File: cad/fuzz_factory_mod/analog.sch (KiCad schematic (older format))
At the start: 25 parts

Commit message: Continued schematic
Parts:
- removed C?: 100n, symbol Device:C
- removed R?: 220k, symbol Device:R
- added C?: 10u, symbol Device:CP
- added C?: 100n, symbol Device:C
- added RV? (x2): 10k, symbol Device:R_POT_TRIM
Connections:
- net labels added: IN_AUDIO
- wire segments 93 -> 100
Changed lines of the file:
@@
-$EndComp
-$Comp
-L Device:C C?
-U 1 1 5DF91F08
-P 4750 4500
-F 0 "C?" V 4498 4500 50  0000 C CNN
-F 1 "100n" V 4589 4500 50  0000 C CNN
-F 2 "" H 4788 4350 50  0001 C CNN
-F 3 "~" H 4750 4500 50  0001 C CNN
-	1    4750 4500
-	0    1    1    0
-$EndComp
-$Comp
-L Device:R R?
-U 1 1 5DF92795
-P 4250 4500
-F 0 "R?" V 4043 4500 50  0000 C CNN
-F 1 "220k" V 4134 4500 50  0000 C CNN
-F 2 "" V 4180 4500 50  0001 C CNN
-F 3 "~" H 4250 4500 50  0001 C CNN
-	1    4250 4500
-	0    1    1    0
 $EndComp
 $Comp
@@
 $EndComp
 Wire Wire Line
-	4400 4500 4600 4500
-Wire Wire Line
 	4900 4500 5000 4500
 Wire Wire Line
@@
 Connection ~ 5000 4500
 Wire Wire Line
-	5000 4500 5200 4500
+	5000 4500 5100 4500
 Wire Wire Line
 	5000 3800 5000 4000
@@
 Wire Wire Line
 	7500 3100 7500 3000
-Wire Wire Line
-	7500 3000 7100 3000
 Connection ~ 7000 3000
 Wire Wire Line
 	7500 3400 7500 3500
-Wire Wire Line
-	7500 3500 7300 3500
 Connection ~ 7000 3500
 Wire Wire Line
 	7000 3500 7000 3600
-Text HLabel 8500 2800 2    50   Input ~ 0
+Text HLabel 1500 7000 0    50   Input ~ 0
 GAIN_POT_1
-Text HLabel 8500 2900 2    50   Input ~ 0
+Text HLabel 1500 7100 0    50   Input ~ 0
 GAIN_POT_2
-Text HLabel 8500 3000 2    50   Input ~ 0
+Text HLabel 1500 7200 0    50   Input ~ 0
 GAIN_POT_3
 Connection ~ 7000 4000
@@
 Wire Wire Line
 	7000 4000 8000 4000
-Text HLabel 8500 2700 2    50   Input ~ 0
+Text HLabel 1500 6500 0    50   Input ~ 0
 COMP_POT_1
-Text HLabel 8500 3100 2    50   Input ~ 0
+Text HLabel 1500 6600 0    50   Input ~ 0
 COMP_POT_2
-Wire Wire Line
-	8500 2700 8000 2700
-Wire Wire Line
-	8000 2700 8000 3000
-Connection ~ 8000 3000
-Wire Wire Line
-	8500 3100 8400 3100
-Wire Wire Line
-	8400 3100 8400 4000
-Wire Wire Line
-	8400 4000 8300 4000
-Connection ~ 8000 4000
-Wire Wire Line
-	8500 2800 7100 2800
-Wire Wire Line
-	7100 2800 7100 3000
-Connection ~ 7100 3000
-Wire Wire Line
-	7100 3000 7000 3000
-Wire Wire Line
-	8500 2900 7300 2900
-Wire Wire Line
-	7300 2900 7300 3500
-Connection ~ 7300 3500
-Wire Wire Line
-	7300 3500 7000 3500
-Wire Wire Line
-	8500 3000 8300 3000
-Wire Wire Line
-	8300 3000 8300 4000
-Connection ~ 8300 4000
-Wire Wire Line
-	8300 4000 8000 4000
 Text Notes 7050 3150 0    50   ~ 0
 DNP
@@
 	7000 5900 7000 6000
 Wire Wire Line
-	6400 5400 6400 5600
-Wire Wire Line
 	6400 6000 7000 6000
 Connection ~ 7000 6000
@@
 Wire Wire Line
 	7000 5100 7000 5000
-Wire Wire Line
-	6400 4900 6400 5000
 Text Notes 7950 3350 1    50   ~ 0
 COMP
@@
 Text HLabel 8500 5200 2    50   Input ~ 0
 VOLUME_POT_3
-Text HLabel 6000 5500 0    50   Input ~ 0
+Text HLabel 1500 6000 0    50   Input ~ 0
 GATE_POT_1
-Text HLabel 6000 5600 0    50   Input ~ 0
+Text HLabel 1500 6100 0    50   Input ~ 0
 GATE_POT_2
-Wire Wire Line
-	6000 5500 6100 5500
-Wire Wire Line
-	6100 5500 6100 5000
-Wire Wire Line
-	6100 5000 6400 5000
-Connection ~ 6400 5000
-Wire Wire Line
-	6400 5000 6400 5100
-Wire Wire Line
-	6000 5600 6400 5600
-Connection ~ 6400 5600
-Wire Wire Line
-	6400 5600 6400 6000
 Wire Wire Line
 	8500 5000 7000 5000
@@
 Wire Wire Line
 	5750 2300 5750 2600
+$Comp
+L Device:R_POT_TRIM RV?
+U 1 1 5DF4B057
+P 2000 3650
+F 0 "RV?" H 1930 3696 50  0000 R CNN
+F 1 "10k" H 1930 3605 50  0000 R CNN
+F 2 "" H 2000 3650 50  0001 C CNN
+F 3 "~" H 2000 3650 50  0001 C CNN
+	1    2000 3650
+	1    0    0    -1
+$EndComp
+Wire Wire Line
+	2000 3800 2000 3850
+Wire Wire Line
+	2150 3650 2200 3650
+Wire Wire Line
+	2200 3650 2200 3850
+Wire Wire Line
+	2200 3850 2000 3850
+Connection ~ 2000 3850
+Text Label 8100 4000 0    50   ~ 0
+COMP_POT_2
+Wire Wire Line
+	7000 3500 7500 3500
+Wire Wire Line
+	7000 3000 7500 3000
+Wire Wire Line
+	8000 4000 8600 4000
+Connection ~ 8000 4000
+Wire Wire Line
+	8000 3000 8600 3000
+Connection ~ 8000 3000
+Text Label 8100 3000 0    50   ~ 0
+COMP_POT_1
+Text Label 7100 3000 0    50   ~ 0
+GAIN_POT_1
+Text Label 7100 3500 0    50   ~ 0
+GAIN_POT_2
+Text Label 7100 4000 0    50   ~ 0
+GAIN_POT_3
+Wire Wire Line
+	6400 4900 6400 5100
+Wire Wire Line
+	6400 5400 6400 6000
+Text Label 6400 5000 0    50   ~ 0
+GATE_POT_1
+Text Label 6400 5500 0    50   ~ 0
+GATE_POT_2
+$Comp
+L Device:CP C?
+U 1 1 5DF7EFC6
+P 4750 4500
+F 0 "C?" H 4868 4546 50  0000 L CNN
+F 1 "10u" H 4868 4455 50  0000 L CNN
+F 2 "" H 4788 4350 50  0001 C CNN
+F 3 "~" H 4750 4500 50  0001 C CNN
+	1    4750 4500
+	0    1    1    0
+$EndComp
+$Comp
+L Device:C C?
+U 1 1 5DF8CBCE
+P 4750 4900
+F 0 "C?" V 4498 4900 50  0000 C CNN
+F 1 "100n" V 4589 4900 50  0000 C CNN
+F 2 "" H 4788 4750 50  0001 C CNN
+F 3 "~" H 4750 4900 50  0001 C CNN
+	1    4750 4900
+	0    -1   -1   0
+$EndComp
+Wire Wire Line
+	4500 4500 4600 4500
+Wire Wire Line
+	4600 4900 4500 4900
+Wire Wire Line
+	4500 4900 4500 4500
+Wire Wire Line
+	4900 4900 5100 4900
+Wire Wire Line
+	5100 4900 5100 4500
+Connection ~ 5100 4500
+Wire Wire Line
+	5100 4500 5200 4500
+Text HLabel 4400 4500 0    50   Input ~ 0
+IN_AUDIO
+Wire Wire Line
+	4400 4500 4500 4500
+Connection ~ 4500 4500
+Text Label 2000 3400 1    50   ~ 0
+COMP_POT_1
+Text Label 2000 3950 3    50   ~ 0
+COMP_POT_2
+$Comp
+L Device:R_POT_TRIM RV?
+U 1 1 5DF95B54
+P 3000 3650
+F 0 "RV?" H 2930 3696 50  0000 R CNN
+F 1 "10k" H 2930 3605 50  0000 R CNN
+F 2 "" H 3000 3650 50  0001 C CNN
+F 3 "~" H 3000 3650 50  0001 C CNN
+	1    3000 3650
+	1    0    0    -1
+$EndComp
+Wire Wire Line
+	3000 3800 3000 3850
+Wire Wire Line
+	3150 3650 3200 3650
+Wire Wire Line
+	3200 3650 3200 3850
+Wire Wire Line
+	3200 3850 3000 3850
+Connection ~ 3000 3850
+Text Label 3000 3400 1    50   ~ 0
+GATE_POT_1
+Text Label 3000 3950 3    50   ~ 0
+GATE_POT_2
+Text Label 1600 6000 0    50   ~ 0
+GATE_POT_1
+Text Label 1600 6100 0    50   ~ 0
+GATE_POT_2
+Text Label 1600 6500 0    50   ~ 0
+COMP_POT_1
+Text Label 1600 6600 0    50   ~ 0
+COMP_POT_2
+Text Label 1600 7000 0    50   ~ 0
+GAIN_POT_1
+Text Label 1600 7100 0    50   ~ 0
+GAIN_POT_2
+Text Label 1600 7200 0    50   ~ 0
+GAIN_POT_3
+Wire Wire Line
+	1500 6000 2100 6000
+Wire Wire Line
+	1500 6100 2100 6100
+Wire Wire Line
+	1500 6500 2100 6500
+Wire Wire Line
+	1500 6600 2100 6600
+Wire Wire Line
+	1500 7000 2100 7000
+Wire Wire Line
+	1500 7100 2100 7100
+Wire Wire Line
+	1500 7200 2100 7200
+Wire Wire Line
+	2000 3850 2000 4500
+Wire Wire Line
+	3000 3850 3000 4500
+Wire Wire Line
+	2000 3500 2000 2900
+Wire Wire Line
+	3000 3500 3000 2900
 $EndSCHEMATC

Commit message: Continued schematic
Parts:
- added R?: 0, symbol Device:R
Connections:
- net labels added: +9V, IN_PWM_LSB, IN_PWM_LSBn, IN_PWM_MSB, IN_PWM_MSBn, OUT_AUDIO, STARVE_POT_1, STARVE_POT_2
- wire segments 100 -> 109
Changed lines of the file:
@@
 $Descr A4 11693 8268
 encoding utf-8
-Sheet 3 5
+Sheet 3 6
 Title ""
 Date ""
@@
 Wire Wire Line
 	7000 3500 7000 3600
+Text HLabel 1500 6900 0    50   Input ~ 0
+GAIN_POT_1
 Text HLabel 1500 7000 0    50   Input ~ 0
-GAIN_POT_1
+GAIN_POT_2
 Text HLabel 1500 7100 0    50   Input ~ 0
-GAIN_POT_2
-Text HLabel 1500 7200 0    50   Input ~ 0
 GAIN_POT_3
 Connection ~ 7000 4000
@@
 Text Label 1600 6600 0    50   ~ 0
 COMP_POT_2
+Text Label 1600 6900 0    50   ~ 0
+GAIN_POT_1
 Text Label 1600 7000 0    50   ~ 0
-GAIN_POT_1
+GAIN_POT_2
 Text Label 1600 7100 0    50   ~ 0
-GAIN_POT_2
-Text Label 1600 7200 0    50   ~ 0
 GAIN_POT_3
 Wire Wire Line
@@
 	1500 6600 2100 6600
 Wire Wire Line
+	1500 6900 2100 6900
+Wire Wire Line
 	1500 7000 2100 7000
 Wire Wire Line
 	1500 7100 2100 7100
 Wire Wire Line
-	1500 7200 2100 7200
-Wire Wire Line
 	2000 3850 2000 4500
 Wire Wire Line
@@
 Wire Wire Line
 	3000 3500 3000 2900
+Text HLabel 1300 1600 0    50   Input ~ 0
+IN_PWM_LSB
+Text HLabel 1300 1700 0    50   Input ~ 0
+IN_PWM_LSBn
+Text HLabel 1300 1800 0    50   Input ~ 0
+IN_PWM_MSB
+Text HLabel 1300 1900 0    50   Input ~ 0
+IN_PWM_MSBn
+Wire Wire Line
+	1500 1600 1300 1600
+Wire Wire Line
+	1300 1700 1500 1700
+Wire Wire Line
+	1500 1800 1300 1800
+Wire Wire Line
+	1300 1900 1500 1900
+$Comp
+L power:+9V #PWR?
+U 1 1 5E01411F
+P 5750 1000
+F 0 "#PWR?" H 5750 850 50  0001 C CNN
+F 1 "+9V" H 5765 1173 50  0000 C CNN
+F 2 "" H 5750 1000 50  0001 C CNN
+F 3 "" H 5750 1000 50  0001 C CNN
+	1    5750 1000
+	1    0    0    -1
+$EndComp
+$Comp
+L Device:R R?
+U 1 1 5E015714
+P 5750 1250
+F 0 "R?" H 5820 1296 50  0000 L CNN
+F 1 "0" H 5820 1205 50  0000 L CNN
+F 2 "" V 5680 1250 50  0001 C CNN
+F 3 "~" H 5750 1250 50  0001 C CNN
+	1    5750 1250
+	1    0    0    -1
+$EndComp
+Wire Wire Line
+	5750 1400 5750 1500
+Connection ~ 5750 1500
+Wire Wire Line
+	5750 1100 5750 1000
+Text Label 5850 1700 0    50   ~ 0
+STARVE_POT_1
+Text Label 5850 2300 0    50   ~ 0
+STARVE_POT_2
+Text Label 1600 7500 0    50   ~ 0
+STARVE_POT_1
+Text Label 1600 7600 0    50   ~ 0
+STARVE_POT_2
+Text HLabel 1500 7500 0    50   Input ~ 0
+STARVE_POT_1
+Text HLabel 1500 7600 0    50   Input ~ 0
+STARVE_POT_2
+Wire Wire Line
+	1500 7500 2100 7500
+Wire Wire Line
+	1500 7600 2100 7600
+Text HLabel 8500 5500 2    50   Input ~ 0
+OUT_AUDIO
+Wire Wire Line
+	8000 5500 8500 5500
+Connection ~ 8000 5500
+$Sheet
+S 7150 800  950  600
+U 5E0DD00B
+F0 "Digipot" 50
+F1 "DIGIPOT.sch" 50
+$EndSheet
 $EndSCHEMATC

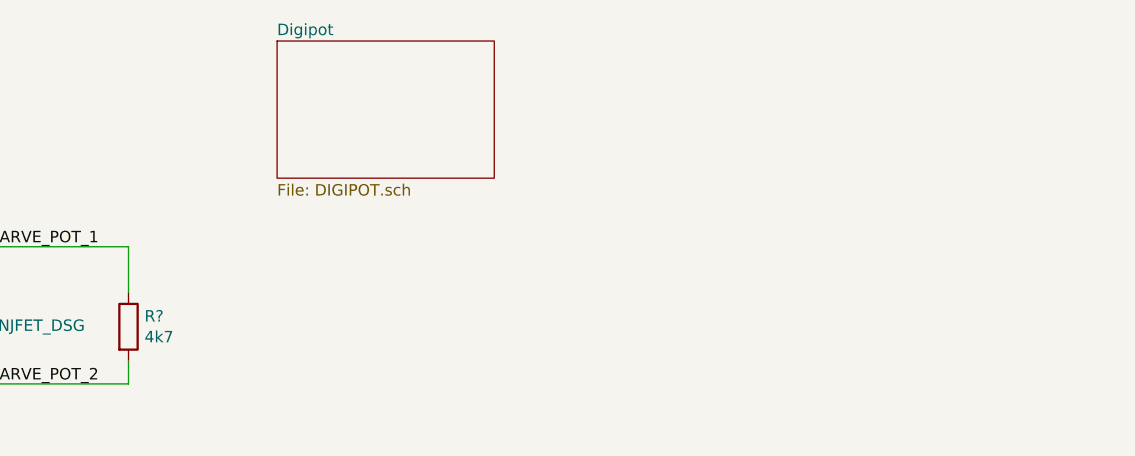
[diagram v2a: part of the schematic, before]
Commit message: Continued schematic.
Added PSU and interface from tremolo project.
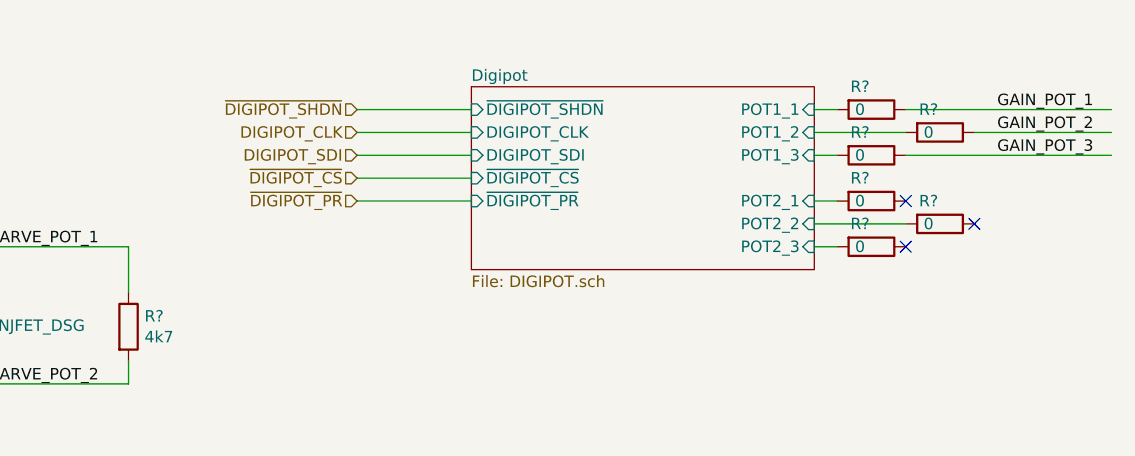
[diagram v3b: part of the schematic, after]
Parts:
- added R? (x6): 0, symbol Device:R
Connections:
- net labels added: DIGIPOT_CLK, DIGIPOT_SDI, ~DIGIPOT_CS, ~DIGIPOT_PR, ~DIGIPOT_SHDN
- wire segments 109 -> 123
- no-connect marks 0 -> 3
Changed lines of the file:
@@
 $Descr A4 11693 8268
 encoding utf-8
-Sheet 3 6
+Sheet 3 11
 Title ""
 Date ""
@@
 Connection ~ 8000 5500
 $Sheet
-S 7150 800  950  600
+S 8000 1000 1500 800
 U 5E0DD00B
 F0 "Digipot" 50
 F1 "DIGIPOT.sch" 50
+F2 "~DIGIPOT_SHDN" I L 8000 1100 50
+F3 "DIGIPOT_CLK" I L 8000 1200 50
+F4 "DIGIPOT_SDI" I L 8000 1300 50
+F5 "~DIGIPOT_CS" I L 8000 1400 50
+F6 "~DIGIPOT_PR" I L 8000 1500 50
+F7 "POT1_1" I R 9500 1100 50
+F8 "POT1_2" I R 9500 1200 50
+F9 "POT1_3" I R 9500 1300 50
+F10 "POT2_1" I R 9500 1500 50
+F11 "POT2_2" I R 9500 1600 50
+F12 "POT2_3" I R 9500 1700 50
 $EndSheet
+Text HLabel 7500 1100 0    50   Input ~ 0
+~DIGIPOT_SHDN
+Text HLabel 7500 1200 0    50   Input ~ 0
+DIGIPOT_CLK
+Text HLabel 7500 1300 0    50   Input ~ 0
+DIGIPOT_SDI
+Text HLabel 7500 1400 0    50   Input ~ 0
+~DIGIPOT_CS
+Text HLabel 7500 1500 0    50   Input ~ 0
+~DIGIPOT_PR
+Wire Wire Line
+	7500 1100 8000 1100
+Wire Wire Line
+	8000 1200 7500 1200
+Wire Wire Line
+	7500 1300 8000 1300
+Wire Wire Line
+	8000 1400 7500 1400
+Wire Wire Line
+	7500 1500 8000 1500
+$Comp
+L Device:R R?
+U 1 1 5E37400A
+P 9750 1100
+F 0 "R?" V 9650 1050 50  0000 C CNN
+F 1 "0" V 9750 1050 50  0000 C CNN
+F 2 "" V 9680 1100 50  0001 C CNN
+F 3 "~" H 9750 1100 50  0001 C CNN
+	1    9750 1100
+	0    1    1    0
+$EndComp
+$Comp
+L Device:R R?
+U 1 1 5E374C21
+P 10050 1200
+F 0 "R?" V 9950 1150 50  0000 C CNN
+F 1 "0" V 10050 1150 50  0000 C CNN
+F 2 "" V 9980 1200 50  0001 C CNN
+F 3 "~" H 10050 1200 50  0001 C CNN
+	1    10050 1200
+	0    1    1    0
+$EndComp
+$Comp
+L Device:R R?
+U 1 1 5E3751A9
+P 9750 1300
+F 0 "R?" V 9650 1250 50  0000 C CNN
+F 1 "0" V 9750 1250 50  0000 C CNN
+F 2 "" V 9680 1300 50  0001 C CNN
+F 3 "~" H 9750 1300 50  0001 C CNN
+	1    9750 1300
+	0    1    1    0
+$EndComp
+$Comp
+L Device:R R?
+U 1 1 5E376867
+P 9750 1500
+F 0 "R?" V 9650 1450 50  0000 C CNN
+F 1 "0" V 9750 1450 50  0000 C CNN
+F 2 "" V 9680 1500 50  0001 C CNN
+F 3 "~" H 9750 1500 50  0001 C CNN
+	1    9750 1500
+	0    1    1    0
+$EndComp
+$Comp
+L Device:R R?
+U 1 1 5E376871
+P 10050 1600
+F 0 "R?" V 9950 1550 50  0000 C CNN
+F 1 "0" V 10050 1550 50  0000 C CNN
+F 2 "" V 9980 1600 50  0001 C CNN
+F 3 "~" H 10050 1600 50  0001 C CNN
+	1    10050 1600
+	0    1    1    0
+$EndComp
+$Comp
+L Device:R R?
+U 1 1 5E37687B
+P 9750 1700
+F 0 "R?" V 9650 1650 50  0000 C CNN
+F 1 "0" V 9750 1650 50  0000 C CNN
+F 2 "" V 9680 1700 50  0001 C CNN
+F 3 "~" H 9750 1700 50  0001 C CNN
+	1    9750 1700
+	0    1    1    0
+$EndComp
+Wire Wire Line
+	9600 1100 9500 1100
+Wire Wire Line
+	9500 1200 9900 1200
+Wire Wire Line
+	9600 1300 9500 1300
+Wire Wire Line
+	9600 1500 9500 1500
+Wire Wire Line
+	9500 1600 9900 1600
+Wire Wire Line
+	9600 1700 9500 1700
+Text Label 10300 1100 0    50   ~ 0
+GAIN_POT_1
+Text Label 10300 1200 0    50   ~ 0
+GAIN_POT_2
+Text Label 10300 1300 0    50   ~ 0
+GAIN_POT_3
+Wire Wire Line
+	10200 1200 10800 1200
+Wire Wire Line
+	9900 1100 10800 1100
+Wire Wire Line
+	9900 1300 10800 1300
+NoConn ~ 9900 1500
+NoConn ~ 10200 1600
+NoConn ~ 9900 1700
 $EndSCHEMATC

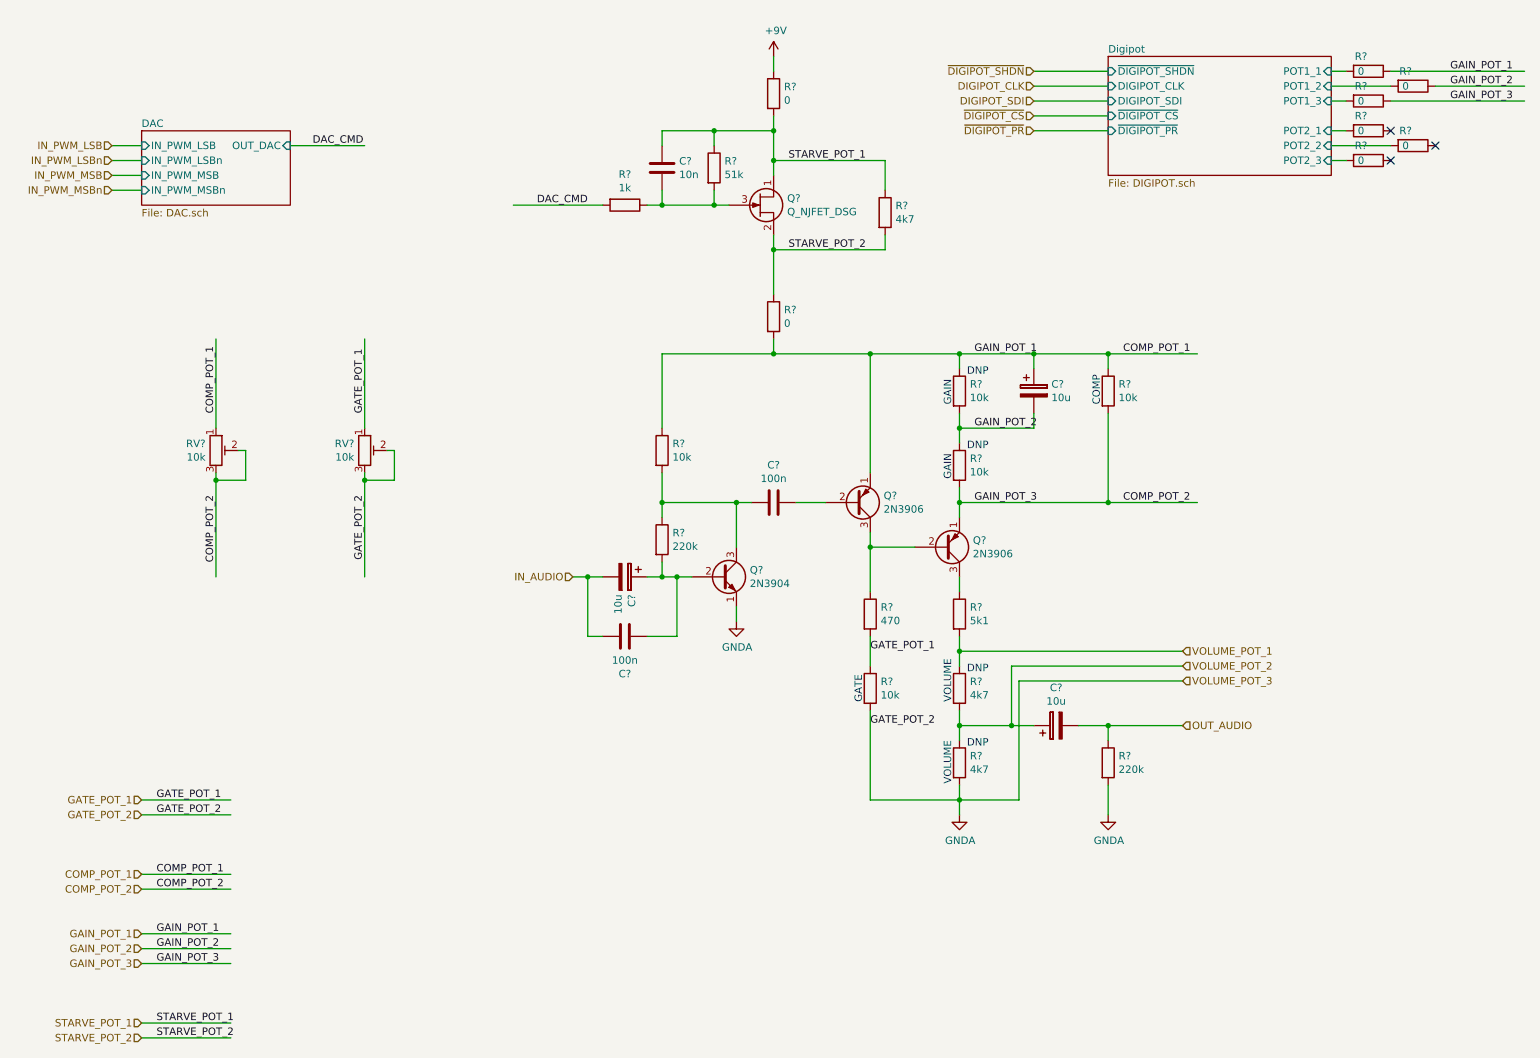
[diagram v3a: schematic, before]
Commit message: Factorised fuzz factory circuit.
Added MIDI interface.
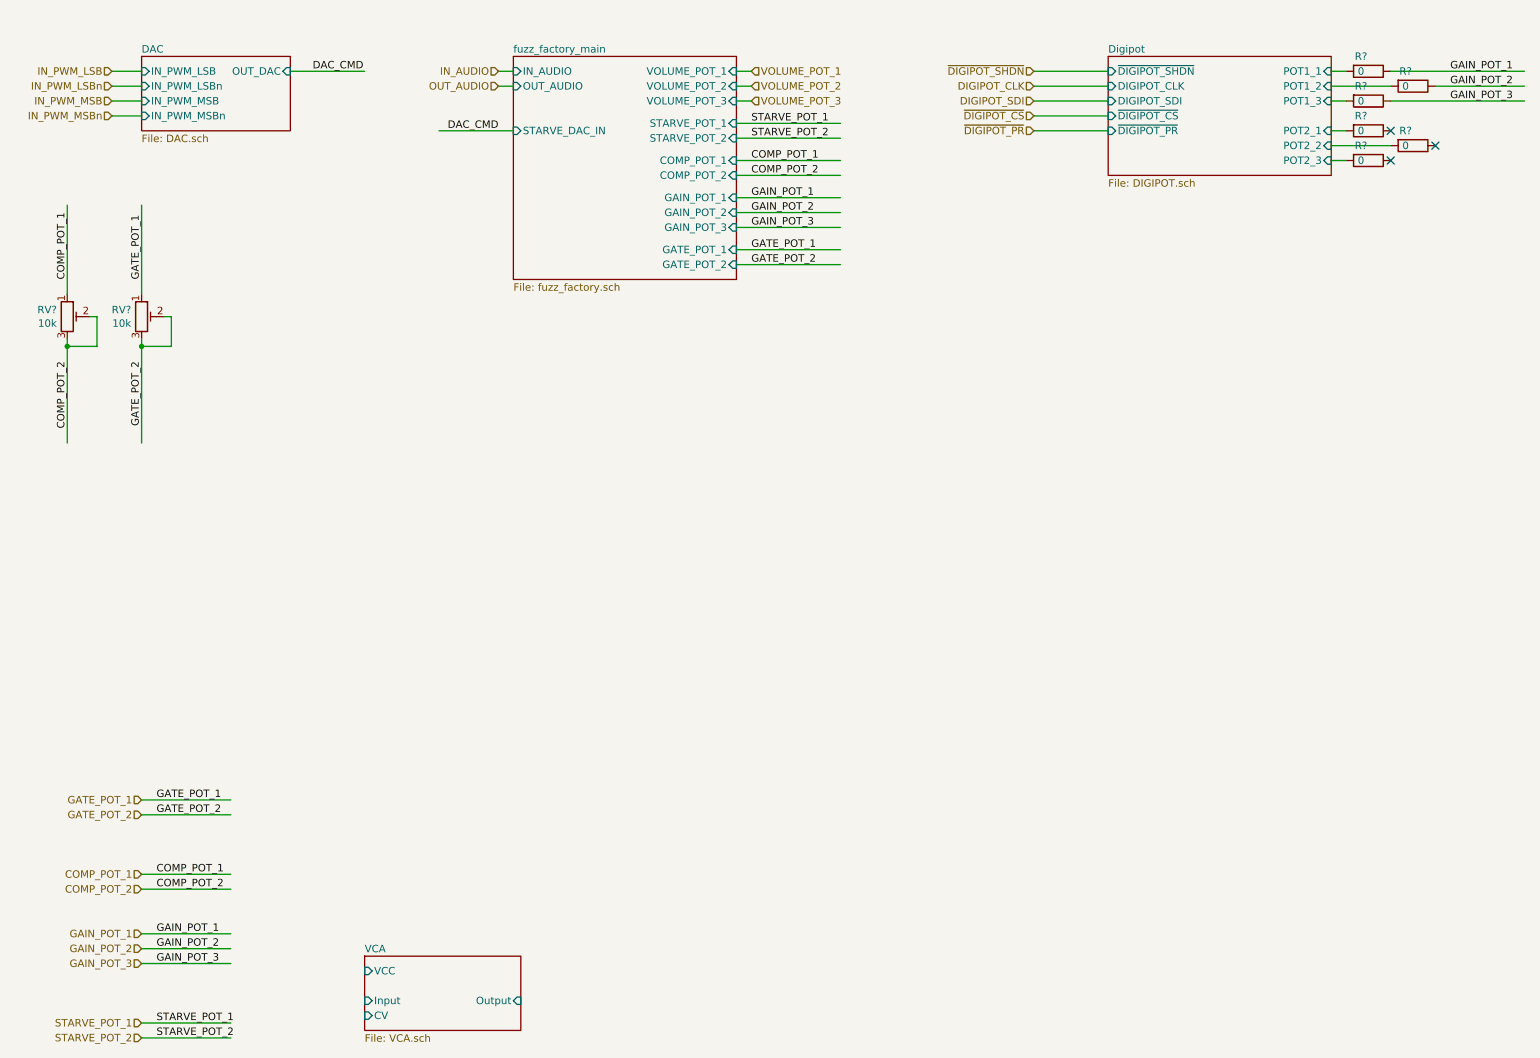
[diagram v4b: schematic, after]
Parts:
- removed C? (x3): 10u, symbol Device:CP
- removed C? (x2): 100n, symbol Device:C
- removed C?: 10n, symbol Device:C
- removed Q?: Q_NJFET_DSG, symbol Device:Q_NJFET_DSG
- removed Q?: 2N3904, Package_TO_SOT_THT:TO-92_Inline, symbol Transistor_BJT:2N3904
- removed Q? (x2): 2N3906, Package_TO_SOT_THT:TO-92_Inline, symbol Transistor_BJT:2N3906
- removed R?: 51k, symbol Device:R
- removed R? (x3): 4k7, symbol Device:R
- removed R?: 1k, symbol Device:R
- removed R? (x5): 10k, symbol Device:R
- removed R? (x2): 220k, symbol Device:R
- removed R?: 5k1, symbol Device:R
- removed R?: 470, symbol Device:R
- removed R? (x2): 0, symbol Device:R
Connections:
- net labels removed: +9V, GNDA
- wire segments 123 -> 55
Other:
- note removed: "COMP"
- note removed: "DNP"
- note removed: "GAIN"
- note removed: "GATE"
- note removed: "VOLUME"
- moved on the sheet: RV?
